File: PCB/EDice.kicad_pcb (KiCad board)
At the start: 2 copper layers, 65 x 30 mm, 24 parts, among them J2 Conn_01x04, J3 Conn_01x04, SW1 SW_Push, U1 PFS154-S16

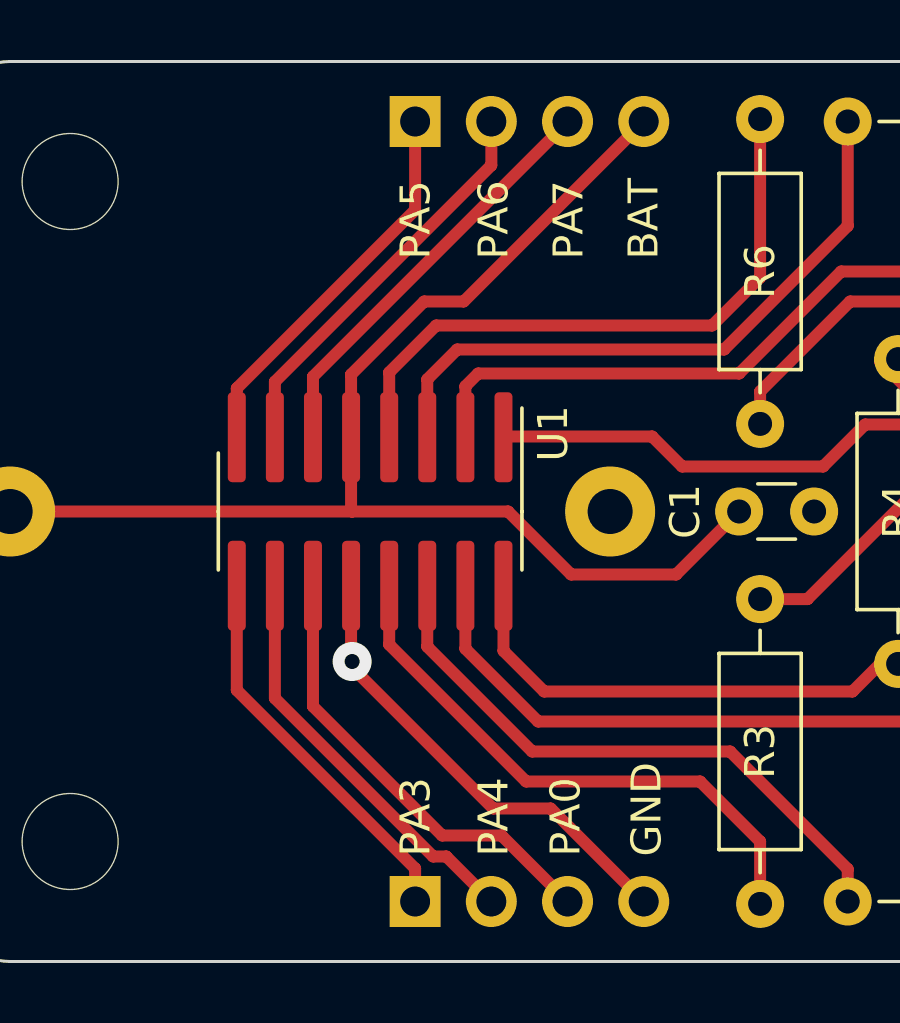
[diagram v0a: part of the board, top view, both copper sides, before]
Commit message: Fixed distance of pin-headers to a multiple of 2.54mm (0.1inch)
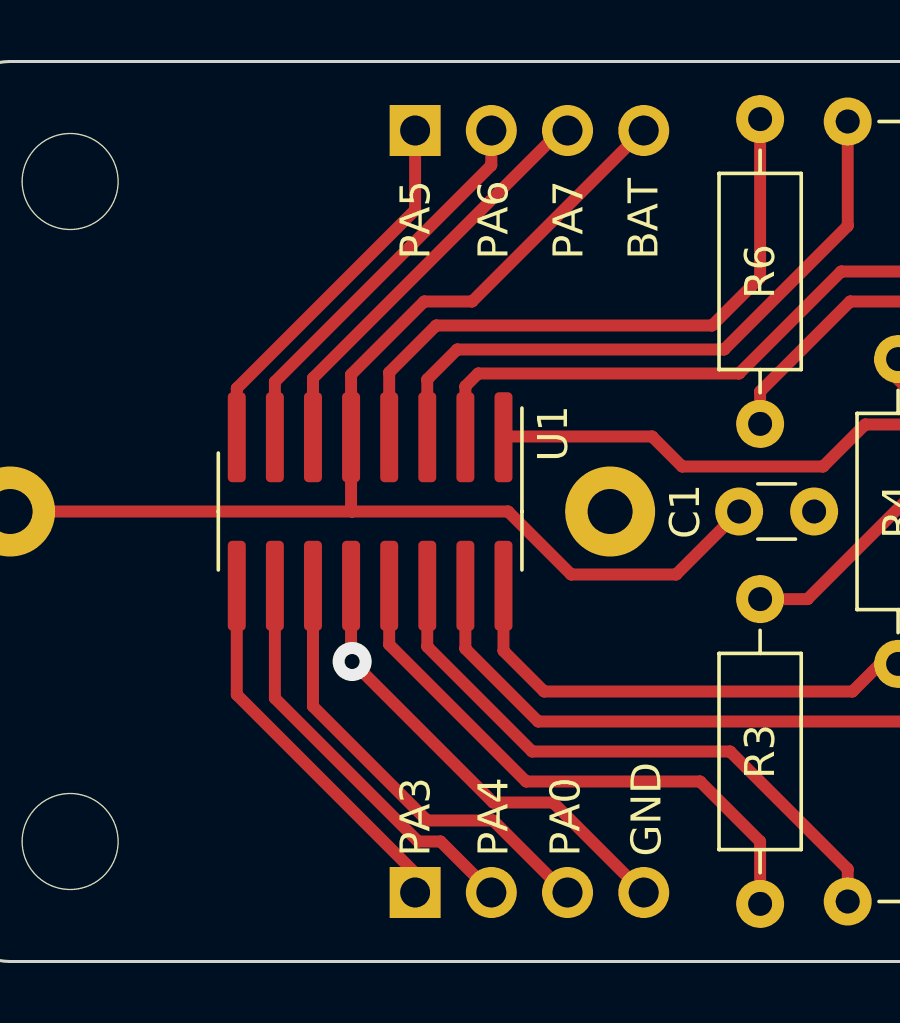
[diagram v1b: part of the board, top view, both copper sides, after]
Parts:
- moved J2 0.30 mm to (108.5, 82.3)
- moved J3 0.30 mm to (108.5, 107.7)
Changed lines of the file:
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@@
   )
   (footprint "Connector_PinHeader_2.54mm:PinHeader_1x04_P2.54mm_Vertical" (layer "B.Cu")
-    (at 108.5 82 -90)
+    (at 108.5 82.3 -90)
     (descr "Through hole straight pin header, 1x04, 2.54mm pitch, single row")
     (tags "Through hole pin header THT 1x04 2.54mm single row")
@@
   )
   (footprint "Connector_PinHeader_2.54mm:PinHeader_1x04_P2.54mm_Vertical" (layer "B.Cu")
-    (at 108.5 108 -90)
+    (at 108.5 107.7 -90)
     (descr "Through hole straight pin header, 1x04, 2.54mm pitch, single row")
     (tags "Through hole pin header THT 1x04 2.54mm single row")
@@
     (effects (font (size 1 1) (thickness 0.15)) (justify left bottom))
   )
-  (segment (start 108.8 88) (end 106.365 90.435) (width 0.4) (layer "F.Cu") (net 1))
-  (segment (start 106.365 90.435) (end 106.365 92.525) (width 0.4) (layer "F.Cu") (net 1))
-  (segment (start 110.12 88) (end 108.8 88) (width 0.4) (layer "F.Cu") (net 1))
   (segment (start 117.2 97.1) (end 113.7 97.1) (width 0.4) (layer "F.Cu") (net 1))
-  (segment (start 116.12 82) (end 110.12 88) (width 0.4) (layer "F.Cu") (net 1))
+  (segment (start 116.12 82.28) (end 110.4 88) (width 0.4) (layer "F.Cu") (net 1))
   (segment (start 113.7 97.1) (end 111.6 95) (width 0.4) (layer "F.Cu") (net 1))
   (segment (start 111.6 95) (end 106.4 95) (width 0.4) (layer "F.Cu") (net 1))
+  (segment (start 106.365 90.435) (end 106.365 92.525) (width 0.4) (layer "F.Cu") (net 1))
   (segment (start 106.4 95) (end 95 95) (width 0.4) (layer "F.Cu") (net 1))
   (segment (start 106.365 92.525) (end 106.365 94.965) (width 0.4) (layer "F.Cu") (net 1))
   (segment (start 119.3 95) (end 117.2 97.1) (width 0.4) (layer "F.Cu") (net 1))
+  (segment (start 110.4 88) (end 108.8 88) (width 0.4) (layer "F.Cu") (net 1))
   (segment (start 106.365 94.965) (end 106.4 95) (width 0.4) (layer "F.Cu") (net 1))
-  (segment (start 111.1 104.9) (end 106.365 100.165) (width 0.4) (layer "F.Cu") (net 2))
+  (segment (start 108.8 88) (end 106.365 90.435) (width 0.4) (layer "F.Cu") (net 1))
+  (segment (start 111.1 104.7) (end 106.4 100) (width 0.4) (layer "F.Cu") (net 2))
   (segment (start 106.365 99.965) (end 106.365 97.475) (width 0.4) (layer "F.Cu") (net 2))
-  (segment (start 116.12 108) (end 113.02 104.9) (width 0.4) (layer "F.Cu") (net 2))
-  (segment (start 113.02 104.9) (end 111.1 104.9) (width 0.4) (layer "F.Cu") (net 2))
-  (segment (start 106.365 100.035) (end 106.4 100) (width 0.4) (layer "F.Cu") (net 2))
-  (segment (start 106.365 100.165) (end 106.365 100.035) (width 0.4) (layer "F.Cu") (net 2))
+  (segment (start 113.1 104.7) (end 111.1 104.7) (width 0.4) (layer "F.Cu") (net 2))
+  (segment (start 116.12 107.72) (end 113.1 104.7) (width 0.4) (layer "F.Cu") (net 2))
   (segment (start 106.4 100) (end 106.365 99.965) (width 0.4) (layer "F.Cu") (net 2))
   (via (at 106.4 100) (size 1.3) (drill 0.5) (layers "F.Cu" "B.Cu") (net 2))
@@
   (segment (start 147.71 101.71) (end 153.08 107.08) (width 0.4) (layer "F.Cu") (net 9))
   (segment (start 146 101.71) (end 147.71 101.71) (width 0.4) (layer "F.Cu") (net 9))
-  (segment (start 105.095 92.525) (end 105.095 90.505) (width 0.4) (layer "F.Cu") (net 10))
-  (segment (start 105.095 90.505) (end 113.58 82.02) (width 0.4) (layer "F.Cu") (net 10))
-  (segment (start 113.58 82.02) (end 113.58 82) (width 0.4) (layer "F.Cu") (net 10))
-  (segment (start 111.04 83.46) (end 111.04 82) (width 0.4) (layer "F.Cu") (net 11))
+  (segment (start 105.095 92.525) (end 105.095 90.555) (width 0.4) (layer "F.Cu") (net 10))
+  (segment (start 105.095 90.555) (end 113.58 82.07) (width 0.4) (layer "F.Cu") (net 10))
+  (segment (start 113.58 82.07) (end 113.58 82) (width 0.4) (layer "F.Cu") (net 10))
   (segment (start 103.825 90.675) (end 111.04 83.46) (width 0.4) (layer "F.Cu") (net 11))
+  (segment (start 111.04 83.46) (end 111.04 82.3) (width 0.4) (layer "F.Cu") (net 11))
   (segment (start 103.825 92.525) (end 103.825 90.675) (width 0.4) (layer "F.Cu") (net 11))
+  (segment (start 102.555 90.895) (end 108.5 84.95) (width 0.4) (layer "F.Cu") (net 12))
+  (segment (start 108.5 84.95) (end 108.5 82.3) (width 0.4) (layer "F.Cu") (net 12))
   (segment (start 102.555 92.525) (end 102.555 90.895) (width 0.4) (layer "F.Cu") (net 12))
-  (segment (start 108.5 84.95) (end 108.5 82) (width 0.4) (layer "F.Cu") (net 12))
-  (segment (start 102.555 90.895) (end 108.5 84.95) (width 0.4) (layer "F.Cu") (net 12))
-  (segment (start 108.5 108) (end 108.5 106.9) (width 0.4) (layer "F.Cu") (net 13))
-  (segment (start 108.5 106.9) (end 102.555 100.955) (width 0.4) (layer "F.Cu") (net 13))
-  (segment (start 102.555 100.955) (end 102.555 97.475) (width 0.4) (layer "F.Cu") (net 13))
-  (segment (start 111.04 108) (end 109.54 106.5) (width 0.4) (layer "F.Cu") (net 14))
+  (segment (start 102.555 101.105) (end 102.555 97.475) (width 0.4) (layer "F.Cu") (net 13))
+  (segment (start 108.5 107.7) (end 108.5 107.05) (width 0.4) (layer "F.Cu") (net 13))
+  (segment (start 108.5 107.05) (end 102.555 101.105) (width 0.4) (layer "F.Cu") (net 13))
   (segment (start 103.825 101.225) (end 103.825 97.475) (width 0.4) (layer "F.Cu") (net 14))
-  (segment (start 109.1 106.5) (end 103.825 101.225) (width 0.4) (layer "F.Cu") (net 14))
-  (segment (start 109.54 106.5) (end 109.1 106.5) (width 0.4) (layer "F.Cu") (net 14))
-  (segment (start 113.58 108) (end 111.38 105.8) (width 0.4) (layer "F.Cu") (net 15))
-  (segment (start 111.38 105.8) (end 109.4 105.8) (width 0.4) (layer "F.Cu") (net 15))
+  (segment (start 111.04 107.69) (end 109.35 106) (width 0.4) (layer "F.Cu") (net 14))
+  (segment (start 109.35 106) (end 108.6 106) (width 0.4) (layer "F.Cu") (net 14))
+  (segment (start 108.6 106) (end 103.825 101.225) (width 0.4) (layer "F.Cu") (net 14))
+  (segment (start 108.9 105.3) (end 105.095 101.495) (width 0.4) (layer "F.Cu") (net 15))
+  (segment (start 111.1 105.3) (end 108.9 105.3) (width 0.4) (layer "F.Cu") (net 15))
+  (segment (start 113.58 107.78) (end 111.1 105.3) (width 0.4) (layer "F.Cu") (net 15))
   (segment (start 105.095 101.495) (end 105.095 97.475) (width 0.4) (layer "F.Cu") (net 15))
-  (segment (start 109.4 105.8) (end 105.095 101.495) (width 0.4) (layer "F.Cu") (net 15))
   (segment (start 108.905 90.595) (end 108.905 92.525) (width 0.4) (layer "F.Cu") (net 16))
   (segment (start 118.8 89.6) (end 109.9 89.6) (width 0.4) (layer "F.Cu") (net 16))

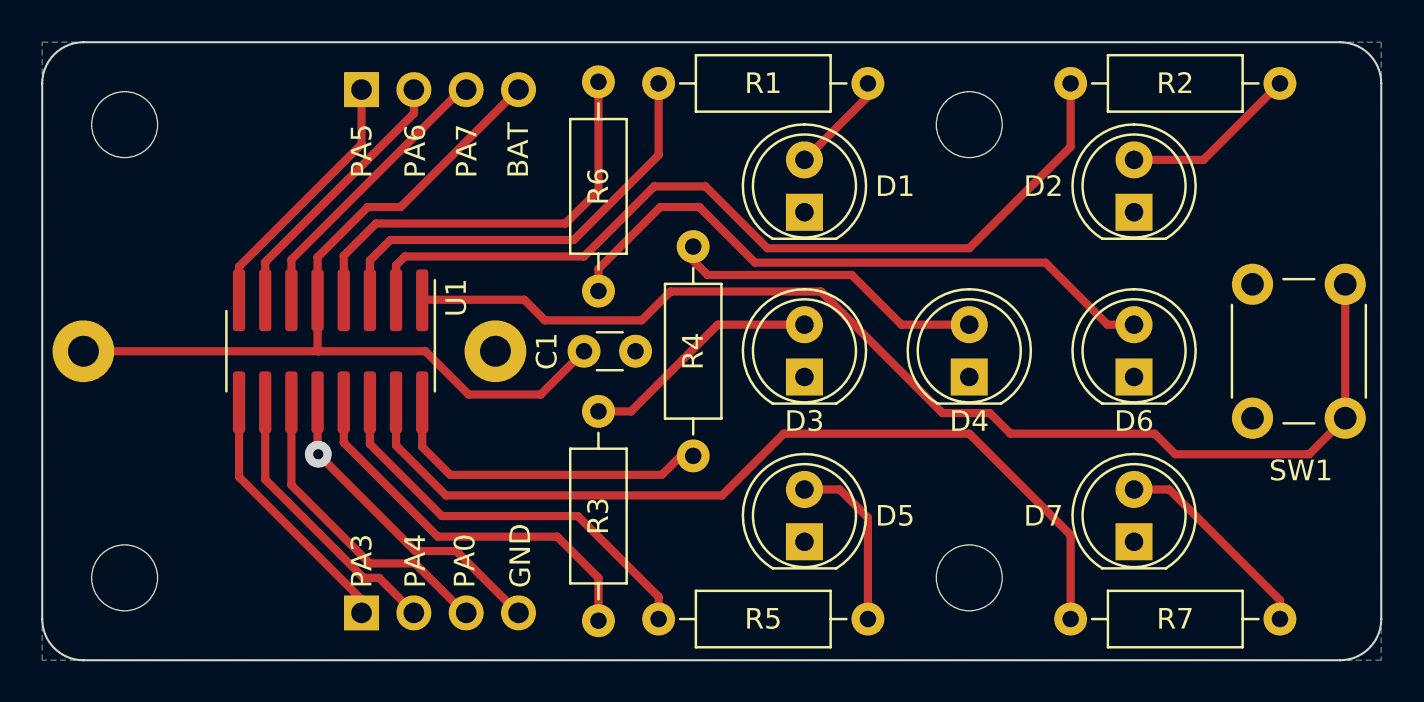
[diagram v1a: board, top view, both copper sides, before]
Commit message: Move screw holes
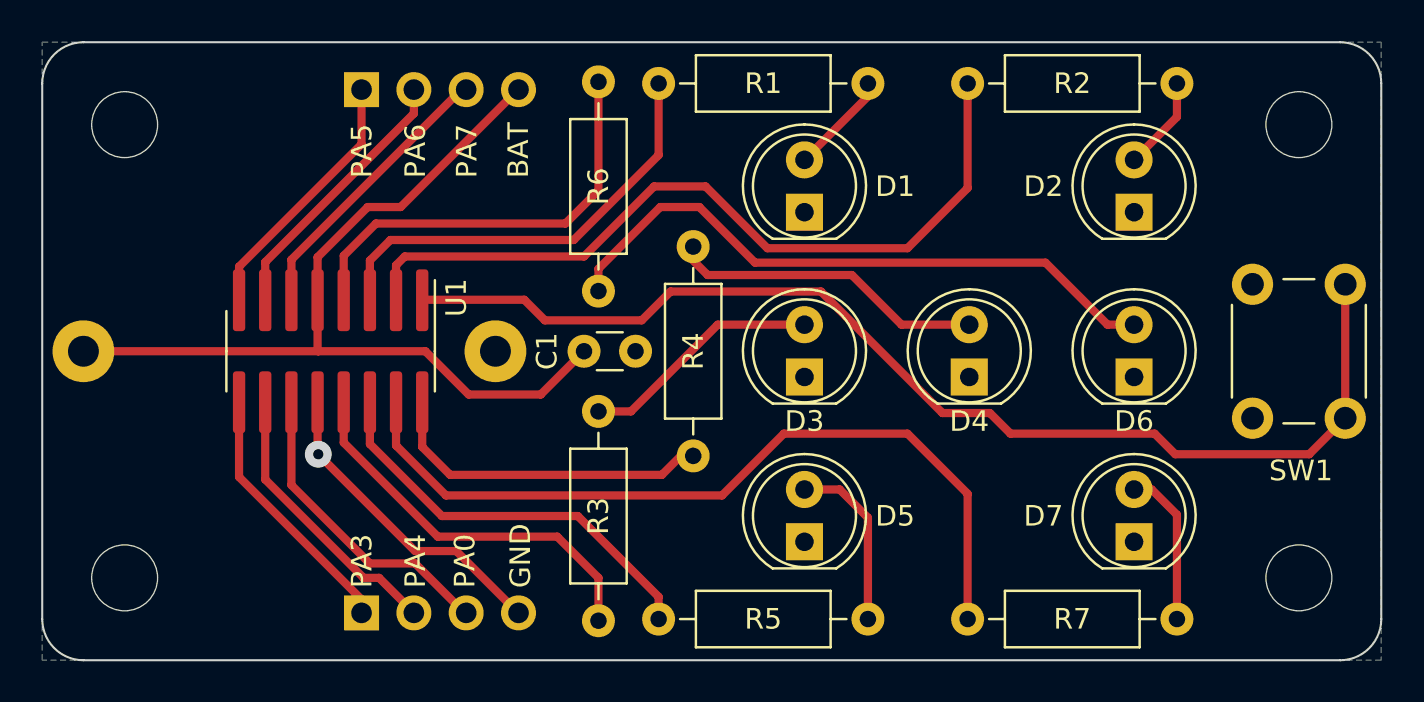
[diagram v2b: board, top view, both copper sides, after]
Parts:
- moved H2 16.0 mm to (154.0, 84.0)
- moved H3 16.0 mm to (154.0, 106.0)
- moved R2 5.00 mm to (137.9, 82.0)
- moved R7 5.00 mm to (137.9, 108.0)
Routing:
- net Net-(D2-A): track 8.62 -> 4.57 mm
- net /LED2: track 42.4 -> 38.6 mm
- net /LED7: track 43.2 -> 39.4 mm
- net Net-(D7-A): track 10.2 -> 7.65 mm
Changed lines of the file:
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@@
   )
   (footprint "MountingHole:MountingHole_3.2mm_M3" (layer "F.Cu")
-    (at 138 84)
+    (at 154 84)
     (descr "Mounting Hole 3.2mm, no annular, M3")
     (tags "mounting hole 3.2mm no annular m3")
@@
   )
   (footprint "Resistor_THT:R_Axial_DIN0207_L6.3mm_D2.5mm_P10.16mm_Horizontal" (layer "F.Cu")
-    (at 142.92 108)
+    (at 137.92 108)
     (descr "Resistor, Axial_DIN0207 series, Axial, Horizontal, pin pitch=10.16mm, 0.25W = 1/4W, length*diameter=6.3*2.5mm^2, http://cdn-reichelt.de/documents/datenblatt/B400/1_4W%23YAG.pdf")
     (tags "Resistor Axial_DIN0207 series Axial Horizontal pin pitch 10.16mm 0.25W = 1/4W length 6.3mm diameter 2.5mm")
@@
   )
   (footprint "MountingHole:MountingHole_3.2mm_M3" (layer "F.Cu")
-    (at 138 106)
+    (at 154 106)
     (descr "Mounting Hole 3.2mm, no annular, M3")
     (tags "mounting hole 3.2mm no annular m3")
@@
   )
   (footprint "Resistor_THT:R_Axial_DIN0207_L6.3mm_D2.5mm_P10.16mm_Horizontal" (layer "F.Cu")
-    (at 142.92 82)
+    (at 137.92 82)
     (descr "Resistor, Axial_DIN0207 series, Axial, Horizontal, pin pitch=10.16mm, 0.25W = 1/4W, length*diameter=6.3*2.5mm^2, http://cdn-reichelt.de/documents/datenblatt/B400/1_4W%23YAG.pdf")
     (tags "Resistor Axial_DIN0207 series Axial Horizontal pin pitch 10.16mm 0.25W = 1/4W length 6.3mm diameter 2.5mm")
@@
   (segment (start 130 85.71) (end 133.08 82.63) (width 0.4) (layer "F.Cu") (net 3))
   (segment (start 133.08 82.63) (end 133.08 82) (width 0.4) (layer "F.Cu") (net 3))
-  (segment (start 149.37 85.71) (end 153.08 82) (width 0.4) (layer "F.Cu") (net 4))
-  (segment (start 146 85.71) (end 149.37 85.71) (width 0.4) (layer "F.Cu") (net 4))
+  (segment (start 148.08 83.63) (end 148.08 82) (width 0.4) (layer "F.Cu") (net 4))
+  (segment (start 146 85.71) (end 148.08 83.63) (width 0.4) (layer "F.Cu") (net 4))
   (segment (start 130 93.71) (end 125.79 93.71) (width 0.4) (layer "F.Cu") (net 5))
   (segment (start 121.58 97.92) (end 120 97.92) (width 0.4) (layer "F.Cu") (net 5))
@@
   (segment (start 127.6 90.7) (end 124.9 88) (width 0.4) (layer "F.Cu") (net 8))
   (segment (start 124.9 88) (end 123 88) (width 0.4) (layer "F.Cu") (net 8))
-  (segment (start 153.08 107.08) (end 153.08 108) (width 0.4) (layer "F.Cu") (net 9))
-  (segment (start 147.71 101.71) (end 153.08 107.08) (width 0.4) (layer "F.Cu") (net 9))
-  (segment (start 146 101.71) (end 147.71 101.71) (width 0.4) (layer "F.Cu") (net 9))
+  (segment (start 148.08 102.935) (end 148.08 108) (width 0.4) (layer "F.Cu") (net 9))
+  (segment (start 146.855 101.71) (end 148.08 102.935) (width 0.4) (layer "F.Cu") (net 9))
+  (segment (start 146 101.71) (end 146.855 101.71) (width 0.4) (layer "F.Cu") (net 9))
   (segment (start 105.095 92.525) (end 105.095 90.555) (width 0.4) (layer "F.Cu") (net 10))
   (segment (start 105.095 90.555) (end 113.58 82.07) (width 0.4) (layer "F.Cu") (net 10))
@@
   (segment (start 109.9 89.6) (end 108.905 90.595) (width 0.4) (layer "F.Cu") (net 16))
   (segment (start 122.92 85.48) (end 118.8 89.6) (width 0.4) (layer "F.Cu") (net 16))
+  (segment (start 119.3 90.4) (end 110.6 90.4) (width 0.4) (layer "F.Cu") (net 17))
+  (segment (start 135 90) (end 128.2 90) (width 0.4) (layer "F.Cu") (net 17))
+  (segment (start 110.175 90.825) (end 110.175 92.525) (width 0.4) (layer "F.Cu") (net 17))
+  (segment (start 125.2 87) (end 122.7 87) (width 0.4) (layer "F.Cu") (net 17))
+  (segment (start 137.92 87.08) (end 135 90) (width 0.4) (layer "F.Cu") (net 17))
+  (segment (start 110.6 90.4) (end 110.175 90.825) (width 0.4) (layer "F.Cu") (net 17))
+  (segment (start 122.7 87) (end 119.3 90.4) (width 0.4) (layer "F.Cu") (net 17))
   (segment (start 128.2 90) (end 125.2 87) (width 0.4) (layer "F.Cu") (net 17))
-  (segment (start 125.2 87) (end 122.7 87) (width 0.4) (layer "F.Cu") (net 17))
-  (segment (start 122.7 87) (end 119.3 90.4) (width 0.4) (layer "F.Cu") (net 17))
-  (segment (start 142.92 82) (end 142.92 85.08) (width 0.4) (layer "F.Cu") (net 17))
-  (segment (start 142.92 85.08) (end 138 90) (width 0.4) (layer "F.Cu") (net 17))
-  (segment (start 110.6 90.4) (end 110.175 90.825) (width 0.4) (layer "F.Cu") (net 17))
-  (segment (start 119.3 90.4) (end 110.6 90.4) (width 0.4) (layer "F.Cu") (net 17))
-  (segment (start 138 90) (end 128.2 90) (width 0.4) (layer "F.Cu") (net 17))
-  (segment (start 110.175 90.825) (end 110.175 92.525) (width 0.4) (layer "F.Cu") (net 17))
+  (segment (start 137.92 82) (end 137.92 87.08) (width 0.4) (layer "F.Cu") (net 17))
   (segment (start 118 104) (end 112.2 104) (width 0.4) (layer "F.Cu") (net 18))
   (segment (start 112.2 104) (end 107.635 99.435) (width 0.4) (layer "F.Cu") (net 18))
@@
   (segment (start 118.4 88.8) (end 109.2 88.8) (width 0.4) (layer "F.Cu") (net 21))
   (segment (start 107.635 90.365) (end 107.635 92.525) (width 0.4) (layer "F.Cu") (net 21))
-  (segment (start 142.92 103.92) (end 138 99) (width 0.4) (layer "F.Cu") (net 22))
-  (segment (start 129 99) (end 126 102) (width 0.4) (layer "F.Cu") (net 22))
-  (segment (start 142.92 108) (end 142.92 103.92) (width 0.4) (layer "F.Cu") (net 22))
-  (segment (start 112.6 102) (end 110.175 99.575) (width 0.4) (layer "F.Cu") (net 22))
-  (segment (start 138 99) (end 129 99) (width 0.4) (layer "F.Cu") (net 22))
-  (segment (start 110.175 99.575) (end 110.175 97.475) (width 0.4) (layer "F.Cu") (net 22))
-  (segment (start 126 102) (end 112.6 102) (width 0.4) (layer "F.Cu") (net 22))
+  (segment (start 137.92 101.92) (end 137.92 108) (width 0.4) (layer "F.Cu") (net 22))
+  (segment (start 112.6 102) (end 126 102) (width 0.4) (layer "F.Cu") (net 22))
+  (segment (start 110.175 99.575) (end 112.6 102) (width 0.4) (layer "F.Cu") (net 22))
+  (segment (start 110.175 97.475) (end 110.175 99.575) (width 0.4) (layer "F.Cu") (net 22))
+  (segment (start 126 102) (end 129 99) (width 0.4) (layer "F.Cu") (net 22))
+  (segment (start 135 99) (end 137.92 101.92) (width 0.4) (layer "F.Cu") (net 22))
+  (segment (start 129 99) (end 135 99) (width 0.4) (layer "F.Cu") (net 22))
   (segment (start 130.8 92.1) (end 123.5 92.1) (width 0.4) (layer "F.Cu") (net 23))
   (segment (start 147 99) (end 140 99) (width 0.4) (layer "F.Cu") (net 23))
